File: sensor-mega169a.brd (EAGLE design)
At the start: 55.6 x 39.9 mm, 55 parts, among them IC3 ATmega169PA, K1 SP6029TOP, M1 NRF24L01P-M, M2 DHT22, Q1 IRLML2502, Q2 IRLML2502, Q3 IRLML6402, U1 MCP1640C, U2 MCP604-I/ST

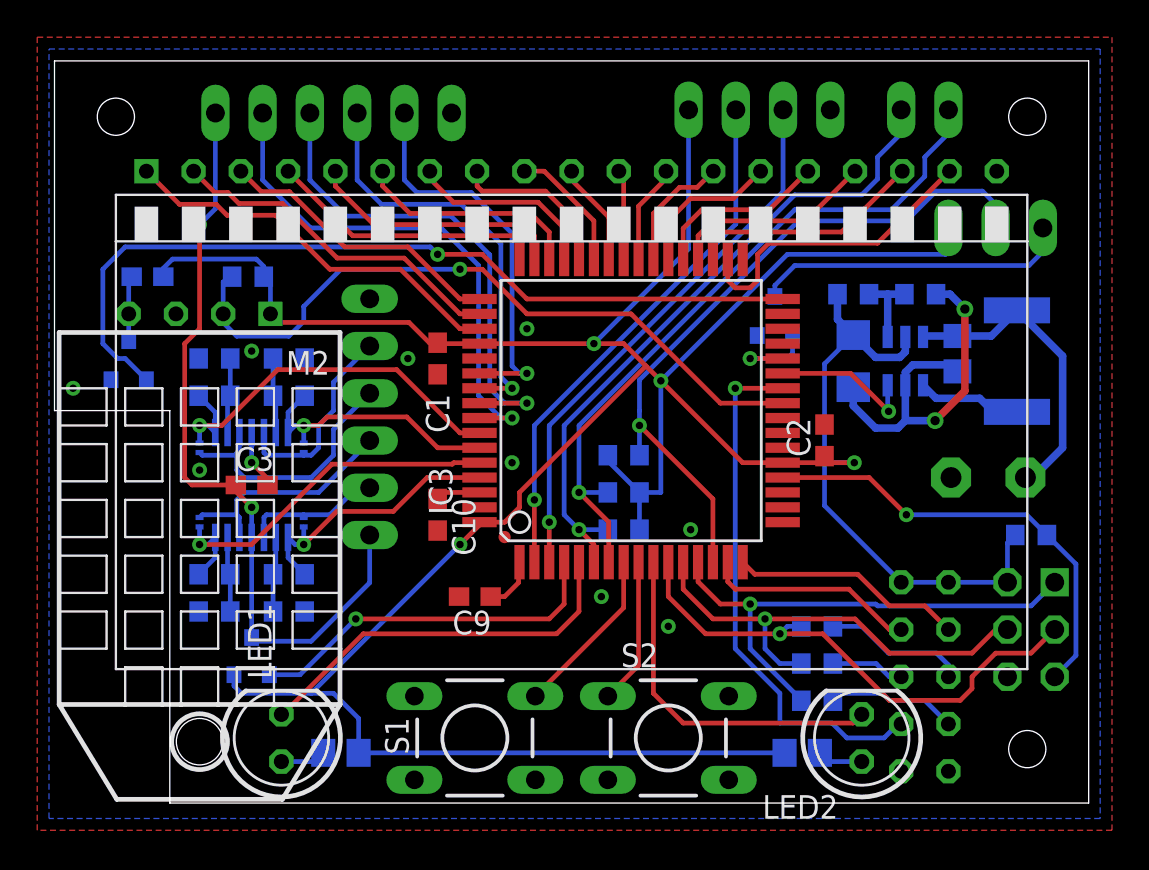
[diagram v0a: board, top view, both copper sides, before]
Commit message: changed irlml* parts to own library with better footprint
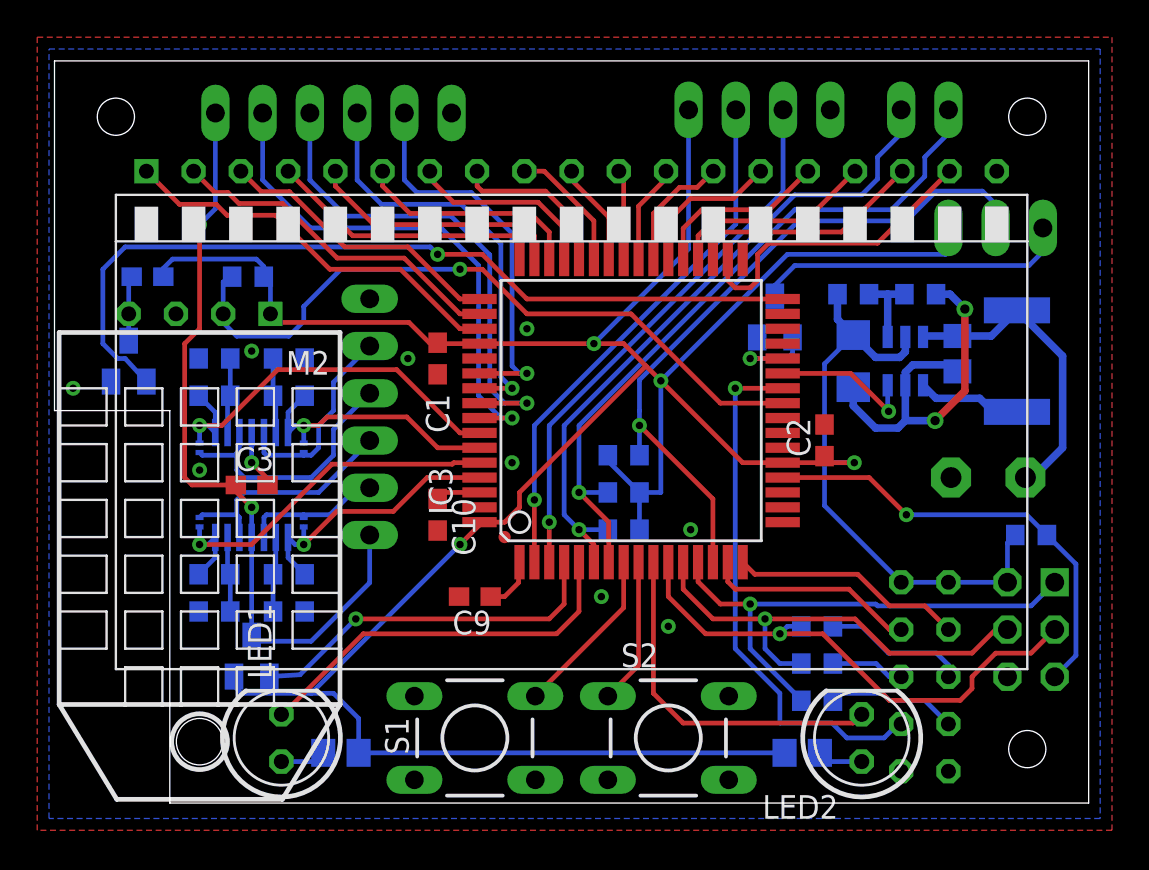
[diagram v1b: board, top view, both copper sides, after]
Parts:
- Q1, Q2: device xmaker:SOT23-3 -> mosfet:MICRO3
- Q3: device transistor-power:MICRO3 -> mosfet:MICRO3
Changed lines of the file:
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@@
 <setting verticaltext="up"/>
 </settings>
-<grid distance="0.4" unitdist="mm" unit="mm" style="lines" multiple="1" display="yes" altdistance="0.1" altunitdist="mm" altunit="mm"/>
+<grid distance="0.05" unitdist="inch" unit="mm" style="lines" multiple="1" display="yes" altdistance="0.025" altunitdist="inch" altunit="mm"/>
 <layers>
 <layer number="1" name="Top" color="4" fill="1" visible="yes" active="yes"/>
@@
 <layer number="21" name="tPlace" color="7" fill="1" visible="no" active="yes"/>
 <layer number="22" name="bPlace" color="7" fill="1" visible="yes" active="yes"/>
-<layer number="23" name="tOrigins" color="15" fill="1" visible="no" active="yes"/>
+<layer number="23" name="tOrigins" color="15" fill="1" visible="yes" active="yes"/>
 <layer number="24" name="bOrigins" color="15" fill="1" visible="yes" active="yes"/>
 <layer number="25" name="tNames" color="7" fill="1" visible="no" active="yes"/>
@@
 <layer number="98" name="Guide" color="6" fill="1" visible="no" active="no"/>
 <layer number="100" name="Muster" color="7" fill="1" visible="no" active="no"/>
+<layer number="101" name="Patch_Top" color="12" fill="4" visible="no" active="yes"/>
+<layer number="102" name="Vscore" color="7" fill="1" visible="no" active="yes"/>
+<layer number="103" name="tMap" color="7" fill="1" visible="yes" active="yes"/>
+<layer number="104" name="Name" color="7" fill="1" visible="yes" active="yes"/>
+<layer number="105" name="tPlate" color="7" fill="1" visible="yes" active="yes"/>
+<layer number="106" name="bPlate" color="7" fill="1" visible="yes" active="yes"/>
+<layer number="107" name="Crop" color="7" fill="1" visible="yes" active="yes"/>
+<layer number="116" name="Patch_BOT" color="9" fill="4" visible="no" active="yes"/>
+<layer number="121" name="_tsilk" color="7" fill="1" visible="no" active="yes"/>
+<layer number="122" name="_bsilk" color="7" fill="1" visible="no" active="yes"/>
+<layer number="151" name="HeatSink" color="7" fill="1" visible="no" active="yes"/>
+<layer number="196" name="aValue" color="7" fill="1" visible="yes" active="yes"/>
 <layer number="200" name="200bmp" color="1" fill="10" visible="no" active="no"/>
+<layer number="201" name="201bmp" color="1" fill="10" visible="yes" active="yes"/>
+<layer number="202" name="202bmp" color="3" fill="10" visible="no" active="yes"/>
+<layer number="203" name="203bmp" color="4" fill="10" visible="no" active="yes"/>
+<layer number="204" name="204bmp" color="5" fill="10" visible="no" active="yes"/>
+<layer number="205" name="205bmp" color="6" fill="10" visible="no" active="yes"/>
+<layer number="206" name="206bmp" color="7" fill="10" visible="no" active="yes"/>
+<layer number="207" name="207bmp" color="8" fill="10" visible="no" active="yes"/>
+<layer number="208" name="208bmp" color="9" fill="10" visible="no" active="yes"/>
 <layer number="250" name="Descript" color="3" fill="1" visible="no" active="no"/>
 <layer number="251" name="SMDround" color="12" fill="11" visible="no" active="no"/>
+<layer number="254" name="cooling" color="7" fill="1" visible="no" active="yes"/>
 </layers>
 <board>
@@
 <element name="R9" library="rcl" package="R0603" value="470k" x="43.145" y="29.46" rot="MR180"/>
 <element name="R10" library="rcl" package="R0603" value="270k" x="46.745" y="29.46" rot="MR0"/>
-<element name="Q1" library="xmaker" package="SOT23-3" value="IRLML2502" x="4.19" y="25.86" rot="MR0"/>
+<element name="Q1" library="mosfet" package="MICRO3" value="IRLML2502" x="4.19" y="25.86" rot="MR0"/>
 <element name="JP1" library="pinhead-mod" package="1X02" value="I2C" x="46.99" y="39.37" rot="MR180"/>
 <element name="JP2" library="pinhead-mod" package="1X03" value="1-Wire" x="50.8" y="33.02" rot="MR180"/>
 <element name="R8" library="rcl" package="R0603" value="4k7" x="30.8" y="16.8" rot="MR0"/>
 <element name="R11" library="rcl" package="R0603" value="4k7" x="30.8" y="18.8" rot="MR0"/>
-<element name="Q2" library="xmaker" package="SOT23-3" value="IRLML2502" x="38.93" y="28.235" rot="MR0"/>
+<element name="Q2" library="mosfet" package="MICRO3" value="IRLML2502" x="38.93" y="28.235" rot="MR0"/>
 <element name="R12" library="rcl" package="R0603" value="4k7" x="30.8" y="20.8" rot="MR180"/>
 <element name="JP3" library="pinhead-mod" package="1X04" value="serial" x="38.1" y="39.37" rot="MR180"/>
@@
 <element name="R23" library="rcl" package="R0201" value="0" x="13.6" y="21.2" rot="MR90"/>
 <element name="R24" library="rcl" package="R0201" value="0" x="8" y="21.2" rot="MR90"/>
-<element name="Q3" library="transistor-power" package="MICRO3" value="IRLML6402" x="10.8" y="10" rot="MR0"/>
+<element name="Q3" library="mosfet" package="MICRO3" value="IRLML6402" x="10.8" y="10" rot="MR0"/>
 <element name="JP4" library="pinhead-mod" package="1X06" value="ADC1" x="17.145" y="22.86" locked="yes" rot="MR90"/>
 <element name="JP5" library="pinhead-mod" package="1X06" value="ADC2" x="15.2" y="39.2" rot="MR180"/>
@@
 <wire x1="32" y1="25.6" x2="30.8" y2="26.8" width="0.254" layer="1"/>
 <wire x1="11.81" y1="28.4" x2="11.81" y2="30.04" width="0.254" layer="16"/>
-<wire x1="9.85" y1="8.4" x2="9.85" y2="9" width="0.254" layer="16"/>
+<wire x1="9.85" y1="8.4" x2="9.85" y2="8.9" width="0.254" layer="16"/>
 <wire x1="6.05" y1="30.4" x2="6.05" y2="30.85" width="0.254" layer="16"/>
 <wire x1="6.05" y1="30.85" x2="6.546" y2="31.346" width="0.254" layer="16"/>
@@
 <wire x1="37.6" y1="26" x2="39.6" y2="26" width="0.254" layer="16"/>
 <wire x1="39.6" y1="26" x2="39.88" y2="26.28" width="0.254" layer="16"/>
-<wire x1="39.88" y1="26.28" x2="39.88" y2="27.235" width="0.254" layer="16"/>
+<wire x1="39.88" y1="26.28" x2="39.88" y2="27.135" width="0.254" layer="16"/>
 </signal>
 <signal name="N$11">
@@
 <wire x1="10.8" y1="18" x2="9.6" y2="19.2" width="0.254" layer="1"/>
 <wire x1="9.6" y1="19.2" x2="9.95" y2="19.2" width="0.254" layer="1"/>
-<wire x1="10.8" y1="16.3806" x2="10.8" y2="11" width="0.254" layer="16"/>
+<wire x1="10.8" y1="16.3806" x2="10.8" y2="11.1" width="0.254" layer="16"/>
 <wire x1="17.145" y1="13.945" x2="14" y2="10.8" width="0.254" layer="16"/>
 <wire x1="14" y1="10.8" x2="11" y2="10.8" width="0.254" layer="16"/>
-<wire x1="11" y1="10.8" x2="10.8" y2="11" width="0.254" layer="16"/>
+<wire x1="11" y1="10.8" x2="10.8" y2="11.1" width="0.254" layer="16"/>
 <wire x1="8" y1="33.2" x2="8" y2="27.6" width="0.254" layer="1"/>
 <wire x1="8" y1="27.6" x2="7.2" y2="26.8" width="0.254" layer="1"/>
@@
 <via x="16.4" y="12" extent="1-16" drill="0.4"/>
 <wire x1="16.4" y1="12" x2="13.4" y2="9" width="0.254" layer="16"/>
-<wire x1="13.4" y1="9" x2="11.75" y2="9" width="0.254" layer="16"/>
+<wire x1="13.4" y1="9" x2="11.75" y2="8.9" width="0.254" layer="16"/>
 <contactref element="IC3" pad="4"/>
 <wire x1="27.6" y1="12.8" x2="27.6" y2="15.05" width="0.254" layer="1"/>
@@
 <wire x1="2.8" y1="26.8" x2="3.6" y2="26" width="0.254" layer="16"/>
 <wire x1="3.6" y1="26" x2="4" y2="26" width="0.254" layer="16"/>
-<wire x1="4" y1="26" x2="5.14" y2="24.86" width="0.254" layer="16"/>
+<wire x1="4" y1="26" x2="5.14" y2="24.76" width="0.254" layer="16"/>
 </signal>
 <signal name="LED1">
@@
 </signal>
 </signals>
-<errors>
-</errors>
 </board>
 </drawing>

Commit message: cc-by-sa license
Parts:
- added U$1: CC-TPLACE-HALF, creative-commons:CC_TPLACE_HS
- added U$3: BY-TPLACE-HS, creative-commons:BY_TPLACE_HS
- added U$4: SA-TPLACE-HALF, creative-commons:SA_TPLACE_HS
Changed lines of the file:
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@@
 <setting verticaltext="up"/>
 </settings>
-<grid distance="0.05" unitdist="inch" unit="mm" style="lines" multiple="1" display="yes" altdistance="0.025" altunitdist="inch" altunit="mm"/>
+<grid distance="0.4" unitdist="mm" unit="mm" style="lines" multiple="1" display="yes" altdistance="0.1" altunitdist="mm" altunit="mm"/>
 <layers>
-<layer number="1" name="Top" color="4" fill="1" visible="yes" active="yes"/>
+<layer number="1" name="Top" color="4" fill="1" visible="no" active="yes"/>
 <layer number="2" name="Route2" color="1" fill="3" visible="no" active="no"/>
 <layer number="3" name="Route3" color="4" fill="3" visible="no" active="no"/>
@@
 <layer number="21" name="tPlace" color="7" fill="1" visible="no" active="yes"/>
 <layer number="22" name="bPlace" color="7" fill="1" visible="yes" active="yes"/>
-<layer number="23" name="tOrigins" color="15" fill="1" visible="yes" active="yes"/>
+<layer number="23" name="tOrigins" color="15" fill="1" visible="no" active="yes"/>
 <layer number="24" name="bOrigins" color="15" fill="1" visible="yes" active="yes"/>
 <layer number="25" name="tNames" color="7" fill="1" visible="no" active="yes"/>
@@
 <element name="JP4" library="pinhead-mod" package="1X06" value="ADC1" x="17.145" y="22.86" locked="yes" rot="MR90"/>
 <element name="JP5" library="pinhead-mod" package="1X06" value="ADC2" x="15.2" y="39.2" rot="MR180"/>
+<element name="U$1" library="creative-commons" package="CC_TPLACE_HS" value="CC-TPLACE-HALF" x="35.6" y="10" rot="MR0"/>
+<element name="U$3" library="creative-commons" package="BY_TPLACE_HS" value="BY-TPLACE-HS" x="30.4" y="10" rot="MR0"/>
+<element name="U$4" library="creative-commons" package="SA_TPLACE_HS" value="SA-TPLACE-HALF" x="25.2" y="10" rot="MR0"/>
 </elements>
 <signals>

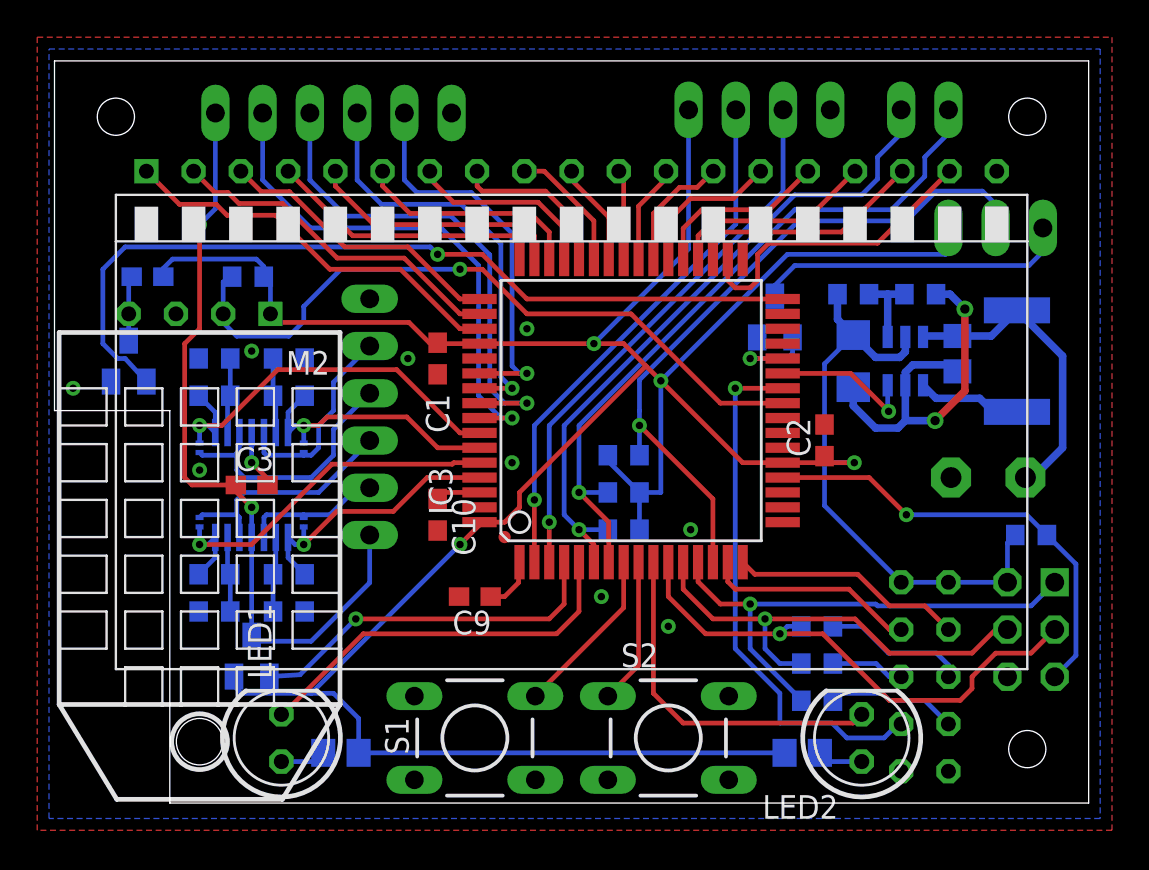
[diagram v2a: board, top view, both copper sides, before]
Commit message: added jumper for spi slave extensions on isp header
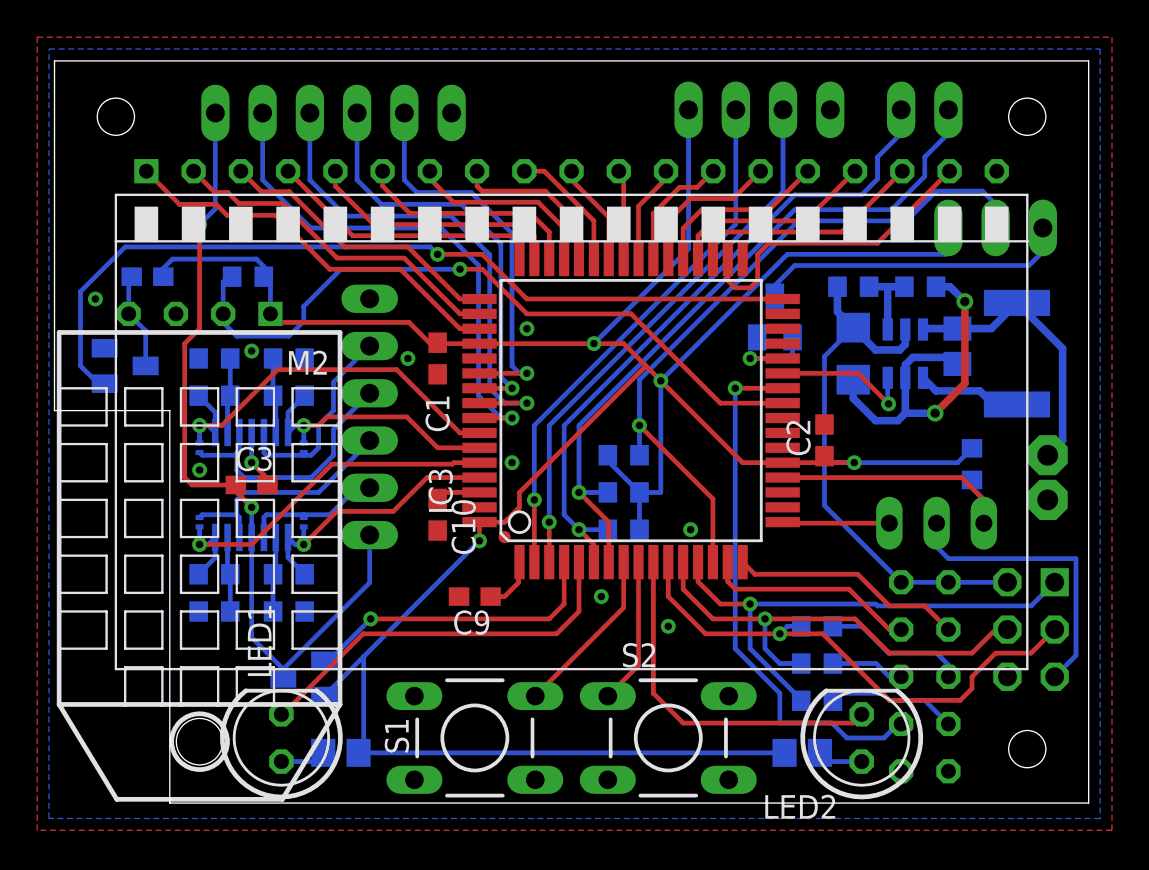
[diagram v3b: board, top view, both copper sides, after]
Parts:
- added JP6: (no value), jumper:JP2
- moved B- 5.34 mm to (53.6, 18.4)
- moved R1 4.96 mm to (49.5, 20.3), turned to 270 degrees
- moved Q3 3.05 mm to (13.6, 8.80), turned to 270 degrees
- moved B+ 1.70 mm to (53.6, 20.8)
- moved C5 0.40 mm to (43.1, 26.3)
- moved L1 0.40 mm to (51.9, 26.3)
- moved U1 0.40 mm to (45.9, 26.3)
- moved C4 0.40 mm to (48.7, 26.7)
- moved R10 0.40 mm to (46.7, 29.9)
- moved R9 0.40 mm to (43.1, 29.9)
- moved Q1 0.32 mm to (4.00, 25.6), turned to 90 degrees
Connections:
- new net N$6: ISP.5, JP6.2
- new net SSEXT: IC3.17, JP6.1
- net !RESET: now also JP6.3; no longer ISP.5
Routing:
- net N$6: track 0.00 -> 15.8 mm
- net !RESET: track 24.2 -> 15.2 mm, vias 1 -> 0
- net SSEXT: track 0.00 -> 5.76 mm
- net ADCON: track 19.7 -> 16.4 mm
- net N$17: track 42.5 -> 44.3 mm
- net N$2: track 3.51 -> 5.24 mm
- net VBAT: track 16.8 -> 15.3 mm
